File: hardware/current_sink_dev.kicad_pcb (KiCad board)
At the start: 2 copper layers, 80 parts, among them J1 USB_C_Receptacle_USB2.0, Q1 TK7S10N1Z, Q3 TK7S10N1Z, U1 AD8602, U10 STM32F042F6Px, U2 ADTL084, U4 ADTL084, U5 PDSE1-S5-D5-M-TR, U6 ADTL084, U7 MIC5504-1.2YM5, U8 MCP4728, U9 DPO2036

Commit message: Began initial routing. Schematic still not fully complete.
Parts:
- removed C1, C2, C22: ?, Capacitor_SMD:C_0805_2012Metric_Pad1.18x1.45mm_HandSolder
- removed C10, C14, C15, C19: 0.1u, Capacitor_SMD:C_0805_2012Metric_Pad1.18x1.45mm_HandSolder
- removed C11: 10u, Capacitor_SMD:C_0805_2012Metric_Pad1.18x1.45mm_HandSolder
- removed C12, C13, C16, C17, C18, C20, C3: 1u, Capacitor_SMD:C_0805_2012Metric_Pad1.18x1.45mm_HandSolder
- removed C7, C8, C9: 4.7u, Capacitor_SMD:C_0805_2012Metric_Pad1.18x1.45mm_HandSolder
- removed H1, H2, H3, H4: ~, MountingHole:MountingHole_3.2mm_M3_Pad_Via
- removed J1: USB_C_Receptacle_USB2.0, Connector_USB:USB_C_Receptacle_Amphenol_12401610E4-2A
- removed J2: ~, Connector_PinHeader_2.54mm:PinHeader_1x02_P2.54mm_Vertical
- removed Q1, Q3: TK7S10N1Z, Package_TO_SOT_SMD:TO-252-2
- removed R1, R37, R50, R7: 0, Resistor_SMD:R_0805_2012Metric_Pad1.20x1.40mm_HandSolder
- removed R10, R53: 1.9k, Resistor_SMD:R_0805_2012Metric_Pad1.20x1.40mm_HandSolder
- removed R11, R3, R43, R44, R45, R46, R48, R49, R5, R52, R54, R6, R9: 10k, Resistor_SMD:R_0805_2012Metric_Pad1.20x1.40mm_HandSolder
- removed R12, R4, R47, R55: 1k, Resistor_SMD:R_0805_2012Metric_Pad1.20x1.40mm_HandSolder
- removed R13, R14, R15, R2, R38, R56, R57, R58: 100, Resistor_SMD:R_0805_2012Metric_Pad1.20x1.40mm_HandSolder
- removed R31, R32, R33, R34: 0R, Resistor_SMD:R_0805_2012Metric_Pad1.20x1.40mm_HandSolder
- removed R35, R36, R39, R40: R_Small, Resistor_SMD:R_0805_2012Metric_Pad1.20x1.40mm_HandSolder
- removed R41, R42: ?, Resistor_SMD:R_0805_2012Metric_Pad1.20x1.40mm_HandSolder
- removed R51, R8: 100m, Resistor_SMD:R_1206_3216Metric_Pad1.30x1.75mm_HandSolder
- removed RV1, RV3: PT10LV05, Potentiometer_THT:Potentiometer_Piher_PT-10-V05_Vertical
- removed U1: AD8602, Package_SO:MSOP-8_3x3mm_P0.65mm
- removed U10: STM32F042F6Px, Package_SO:TSSOP-20_4.4x6.5mm_P0.65mm
- removed U2, U4, U6: ADTL084, Package_SO:SOIC-14_3.9x8.7mm_P1.27mm
- removed U5: PDSE1-S5-D5-M-TR, User_SupplyGen:PDS1-M
- removed U7: MIC5504-1.2YM5, Package_TO_SOT_SMD:SOT-23-5_HandSoldering
- removed U8: MCP4728, Package_SO:MSOP-10_3x3mm_P0.5mm
- removed U9: DPO2036, User_USB_Protection:UQFN2020-12
- added C100: 4.7u, Capacitor_SMD:C_0805_2012Metric_Pad1.18x1.45mm_HandSolder, B.Cu at (207.5, 32.5)
- added C101: 4.7u, Capacitor_SMD:C_0805_2012Metric_Pad1.18x1.45mm_HandSolder, B.Cu at (214.0, 32.5)
- added C102: 4.7u, Capacitor_SMD:C_0805_2012Metric_Pad1.18x1.45mm_HandSolder, B.Cu at (203.5, 32.5)
- added C200: ?, Capacitor_SMD:C_0805_2012Metric_Pad1.18x1.45mm_HandSolder, F.Cu at (134.0, 97.5)
- added C201: ?, Capacitor_SMD:C_0805_2012Metric_Pad1.18x1.45mm_HandSolder, B.Cu at (133.5, 127.5)
- added C202: ?, Capacitor_SMD:C_0805_2012Metric_Pad1.18x1.45mm_HandSolder, F.Cu at (134.0, 103.5)
- added C203: 1u, Capacitor_SMD:C_0805_2012Metric_Pad1.18x1.45mm_HandSolder, F.Cu at (128.0, 130.0)
- added C204: 1u, Capacitor_SMD:C_0805_2012Metric_Pad1.18x1.45mm_HandSolder, F.Cu at (128.0, 150.0)
- added C300: 1u, Capacitor_SMD:C_0805_2012Metric_Pad1.18x1.45mm_HandSolder, B.Cu at (258.0, 64.0)
- added C400: 0.1u, Capacitor_SMD:C_0805_2012Metric_Pad1.18x1.45mm_HandSolder, F.Cu at (148.8, 75.4)
- added C401: 10u, Capacitor_SMD:C_0805_2012Metric_Pad1.18x1.45mm_HandSolder, F.Cu at (148.8, 78.4)
- added C402: 1u, Capacitor_SMD:C_0805_2012Metric_Pad1.18x1.45mm_HandSolder, F.Cu at (228.0, 76.0)
- added C403: 1u, Capacitor_SMD:C_0805_2012Metric_Pad1.18x1.45mm_HandSolder, F.Cu at (236.0, 76.0)
- added C404: 0.1u, Capacitor_SMD:C_0805_2012Metric_Pad1.18x1.45mm_HandSolder, F.Cu at (148.8, 87.4)
- added C405: 0.1u, Capacitor_SMD:C_0805_2012Metric_Pad1.18x1.45mm_HandSolder, F.Cu at (153.6, 75.4)
- added C406: 1u, Capacitor_SMD:C_0805_2012Metric_Pad1.18x1.45mm_HandSolder, F.Cu at (153.6, 78.4)
- added C407: 1u, Capacitor_SMD:C_0805_2012Metric_Pad1.18x1.45mm_HandSolder, F.Cu at (153.6, 81.4)
- added C408: 1u, Capacitor_SMD:C_0805_2012Metric_Pad1.18x1.45mm_HandSolder, F.Cu at (153.6, 84.4)
- added C409: 0.1u, Capacitor_SMD:C_0805_2012Metric_Pad1.18x1.45mm_HandSolder, F.Cu at (153.6, 87.4)
- added H500: ~, MountingHole:MountingHole_3.2mm_M3_Pad_Via, F.Cu at (225.0, 119.0)
- added H501: ~, MountingHole:MountingHole_3.2mm_M3_Pad_Via, F.Cu at (192.5, 32.5)
- added H502: ~, MountingHole:MountingHole_3.2mm_M3_Pad_Via, F.Cu at (192.5, 117.5)
- added H503: ~, MountingHole:MountingHole_3.2mm_M3_Pad_Via, F.Cu at (257.5, 117.5)
- added H504: ~, MountingHole:MountingHole_3.2mm_M3_Pad_Via, F.Cu at (257.5, 32.5)
- added H505: ~, MountingHole:MountingHole_3.2mm_M3_Pad_Via, F.Cu at (225.0, 109.0)
- added J100: USB_C_Receptacle_USB2.0, Connector_USB:USB_C_Receptacle_Amphenol_12401610E4-2A, F.Cu at (240.5, 29.2)
- added J500: Conn_01x01_Socket, Connector:Banana_Cliff_FCR7350x_S16N-PC_Horizontal, F.Cu at (212.5, 115.0)
- added J501: Conn_01x01_Socket, Connector:Banana_Cliff_FCR7350x_S16N-PC_Horizontal, F.Cu at (237.5, 115.0)
- added J502: ~, Connector_PinHeader_2.54mm:PinHeader_1x02_P2.54mm_Vertical, F.Cu at (57.2, 74.1)
- added Q200: TK7S10N1Z, Package_TO_SOT_SMD:TO-252-2, F.Cu at (167.2, 96.9)
- added Q201: TK7S10N1Z, Package_TO_SOT_SMD:TO-252-2, F.Cu at (167.2, 106.3)
- added R100: 0R, Resistor_SMD:R_0805_2012Metric_Pad1.20x1.40mm_HandSolder, F.Cu at (199.5, 36.0)
- added R200: 0, Resistor_SMD:R_0805_2012Metric_Pad1.20x1.40mm_HandSolder, F.Cu at (102.8, 87.2)
- added R201: 100, Resistor_SMD:R_0805_2012Metric_Pad1.20x1.40mm_HandSolder, F.Cu at (102.8, 90.2)
- added R202: 10k, Resistor_SMD:R_0805_2012Metric_Pad1.20x1.40mm_HandSolder, F.Cu at (128.0, 124.5)
- added R203: 1k, Resistor_SMD:R_0805_2012Metric_Pad1.20x1.40mm_HandSolder, F.Cu at (102.8, 96.1)
- added R204: 10k, Resistor_SMD:R_0805_2012Metric_Pad1.20x1.40mm_HandSolder, F.Cu at (126.0, 124.5)
- added R205: 10k, Resistor_SMD:R_0805_2012Metric_Pad1.20x1.40mm_HandSolder, F.Cu at (126.0, 130.0)
- added R206: 0, Resistor_SMD:R_0805_2012Metric_Pad1.20x1.40mm_HandSolder, F.Cu at (143.0, 130.0)
- added R207: 100m, Resistor_SMD:R_1206_3216Metric_Pad1.30x1.75mm_HandSolder, F.Cu at (110.0, 113.3)
- added R208: 10k, Resistor_SMD:R_0805_2012Metric_Pad1.20x1.40mm_HandSolder, F.Cu at (141.0, 130.0)
- added R209: 1.9k, Resistor_SMD:R_0805_2012Metric_Pad1.20x1.40mm_HandSolder, F.Cu at (115.5, 124.5)
- added R210: 10k, Resistor_SMD:R_0805_2012Metric_Pad1.20x1.40mm_HandSolder, F.Cu at (139.0, 130.0)
- added R211: 1k, Resistor_SMD:R_0805_2012Metric_Pad1.20x1.40mm_HandSolder, F.Cu at (117.5, 124.5)
- added R212: 100, Resistor_SMD:R_0805_2012Metric_Pad1.20x1.40mm_HandSolder, F.Cu at (119.5, 124.5)
- added R213: 100, Resistor_SMD:R_0805_2012Metric_Pad1.20x1.40mm_HandSolder, F.Cu at (115.5, 128.5)
- added R214: 100, Resistor_SMD:R_0805_2012Metric_Pad1.20x1.40mm_HandSolder, F.Cu at (117.5, 128.5)
- added R215: 0, Resistor_SMD:R_0805_2012Metric_Pad1.20x1.40mm_HandSolder, F.Cu at (107.6, 104.9)
- added R216: 100, Resistor_SMD:R_0805_2012Metric_Pad1.20x1.40mm_HandSolder, F.Cu at (107.6, 107.9)
- added R217: 10k, Resistor_SMD:R_0805_2012Metric_Pad1.20x1.40mm_HandSolder, F.Cu at (128.0, 144.5)
- added R218: 1k, Resistor_SMD:R_0805_2012Metric_Pad1.20x1.40mm_HandSolder, F.Cu at (112.3, 90.2)
- added R219: 10k, Resistor_SMD:R_0805_2012Metric_Pad1.20x1.40mm_HandSolder, F.Cu at (126.0, 144.5)
- added R220: 10k, Resistor_SMD:R_0805_2012Metric_Pad1.20x1.40mm_HandSolder, F.Cu at (126.0, 150.0)
- added R221: 0, Resistor_SMD:R_0805_2012Metric_Pad1.20x1.40mm_HandSolder, F.Cu at (143.0, 150.0)
- added R222: 100m, Resistor_SMD:R_1206_3216Metric_Pad1.30x1.75mm_HandSolder, F.Cu at (110.0, 116.0)
- added R223: 10k, Resistor_SMD:R_0805_2012Metric_Pad1.20x1.40mm_HandSolder, F.Cu at (141.0, 150.0)
- added R224: 1.9k, Resistor_SMD:R_0805_2012Metric_Pad1.20x1.40mm_HandSolder, F.Cu at (104.5, 124.5)
- added R225: 10k, Resistor_SMD:R_0805_2012Metric_Pad1.20x1.40mm_HandSolder, F.Cu at (139.0, 150.0)
- added R226: 1k, Resistor_SMD:R_0805_2012Metric_Pad1.20x1.40mm_HandSolder, F.Cu at (102.5, 124.5)
- added R227: 100, Resistor_SMD:R_0805_2012Metric_Pad1.20x1.40mm_HandSolder, F.Cu at (100.5, 124.5)
- added R228: 100, Resistor_SMD:R_0805_2012Metric_Pad1.20x1.40mm_HandSolder, F.Cu at (104.5, 128.5)
- added R229: 100, Resistor_SMD:R_0805_2012Metric_Pad1.20x1.40mm_HandSolder, F.Cu at (102.5, 128.5)
- added R400: ?, Resistor_SMD:R_0805_2012Metric_Pad1.20x1.40mm_HandSolder, F.Cu at (158.4, 75.3)
- added R401: ?, Resistor_SMD:R_0805_2012Metric_Pad1.20x1.40mm_HandSolder, F.Cu at (158.4, 78.3)
- added R402: 10k, Resistor_SMD:R_0805_2012Metric_Pad1.20x1.40mm_HandSolder, F.Cu at (158.4, 81.2)
- added R403: 10k, Resistor_SMD:R_0805_2012Metric_Pad1.20x1.40mm_HandSolder, F.Cu at (158.4, 84.2)
- added R404: 10k, Resistor_SMD:R_0805_2012Metric_Pad1.20x1.40mm_HandSolder, F.Cu at (158.4, 87.1)
- added R500: 0R, Resistor_SMD:R_0805_2012Metric_Pad1.20x1.40mm_HandSolder, F.Cu at (145.0, 124.5)
- added R501: 0R, Resistor_SMD:R_0805_2012Metric_Pad1.20x1.40mm_HandSolder, F.Cu at (143.0, 124.5)
- added R502: R_Small, Resistor_SMD:R_0805_2012Metric_Pad1.20x1.40mm_HandSolder, F.Cu at (139.0, 124.5)
- added R503: R_Small, Resistor_SMD:R_0805_2012Metric_Pad1.20x1.40mm_HandSolder, F.Cu at (141.0, 124.5)
- added R504: 0R, Resistor_SMD:R_0805_2012Metric_Pad1.20x1.40mm_HandSolder, F.Cu at (145.0, 144.5)
- added R505: 0R, Resistor_SMD:R_0805_2012Metric_Pad1.20x1.40mm_HandSolder, F.Cu at (143.0, 144.5)
- added R506: R_Small, Resistor_SMD:R_0805_2012Metric_Pad1.20x1.40mm_HandSolder, F.Cu at (139.0, 144.5)
- added R507: R_Small, Resistor_SMD:R_0805_2012Metric_Pad1.20x1.40mm_HandSolder, F.Cu at (141.0, 144.5)
- added RV200: PT10LV05, Potentiometer_THT:Potentiometer_Piher_PT-10-V05_Vertical, F.Cu at (103.9, 82.3)
- added RV201: PT10LV05, Potentiometer_THT:Potentiometer_Piher_PT-10-V05_Vertical, F.Cu at (115.8, 82.3)
- added RV300: PT10LV05, Potentiometer_THT:Potentiometer_Piher_PT-10-V05_Vertical, B.Cu at (255.5, 51.5)
- added S300: VIM-878-DP-RC-S-LV, User_LDC_Display:VIM878DPRCSLV, F.Cu at (225.0, 55.0)
- added SW500: RotaryEncoder_Switch, Rotary_Encoder:RotaryEncoder_Alps_EC11E-Switch_Vertical_H20mm, F.Cu at (244.8, 88.8)
- added U100: PDSE1-S5-D5-M-TR, User_SupplyGen:PDS1-M, F.Cu at (210.2, 32.5)
- added U200: AD8602, Package_SO:MSOP-8_3x3mm_P0.65mm, F.Cu at (110.0, 126.0)
- added U201: ADTL084, Package_SO:SOIC-14_3.9x8.7mm_P1.27mm, F.Cu at (133.5, 127.3)
- added U202: ADTL084, Package_SO:SOIC-14_3.9x8.7mm_P1.27mm, F.Cu at (133.5, 147.5)
- added U300: BU9797A, Package_SO:TSSOP-48_8x12.5mm_P0.5mm, B.Cu at (225.0, 55.0)
- added U400: MIC5504-1.2YM5, Package_TO_SOT_SMD:SOT-23-5_HandSoldering, F.Cu at (232.0, 76.0)
- added U401: MCP4728, Package_SO:MSOP-10_3x3mm_P0.5mm, F.Cu at (237.1, 84.7)
- added U402: DPO2036, User_USB_Protection:UQFN2020-12, F.Cu at (225.5, 32.2)
- added U403: STM32F042F6Px, Package_SO:TSSOP-20_4.4x6.5mm_P0.65mm, F.Cu at (282.5, 87.0)
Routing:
- net /LCD_screen/disp36_dig_l: track 0.00 -> 48.4 mm, vias 0 -> 2
- net /LCD_screen/disp35_dig_l: track 0.00 -> 45.7 mm, vias 0 -> 2
- net /LCD_screen/disp1_dig_l: track 0.00 -> 45.7 mm, vias 0 -> 2
- net /LCD_screen/disp2_dig_l: track 0.00 -> 43.0 mm, vias 0 -> 2
- net /LCD_screen/disp34_dig_l: track 0.00 -> 40.6 mm, vias 0 -> 2
- net /LCD_screen/disp3_dig_l: track 0.00 -> 38.8 mm, vias 0 -> 2
- net /LCD_screen/disp4_dig_l: track 0.00 -> 37.5 mm, vias 0 -> 2
- net /LCD_screen/disp5_dig_l: track 0.00 -> 36.4 mm, vias 0 -> 2
- net /LCD_screen/disp33_dig_l: track 0.00 -> 35.6 mm, vias 0 -> 2
- net /LCD_screen/COM1_dig_l: track 0.00 -> 33.2 mm, vias 0 -> 2
- net /LCD_screen/COM0_dig_l: track 0.00 -> 32.8 mm, vias 0 -> 2
- net /LCD_screen/disp6_dig_l: track 0.00 -> 30.4 mm, vias 0 -> 2
- net /LCD_screen/disp32_dig_l: track 0.00 -> 30.2 mm, vias 0 -> 2
- net /LCD_screen/disp21_dig_l: track 0.00 -> 28.3 mm
- net /LCD_screen/disp16_dig_l: track 0.00 -> 27.6 mm
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- added copper zone on B.Cu, net GND
- added copper zone on F.Cu, net GND
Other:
- board outline added: 80 x 100 mm

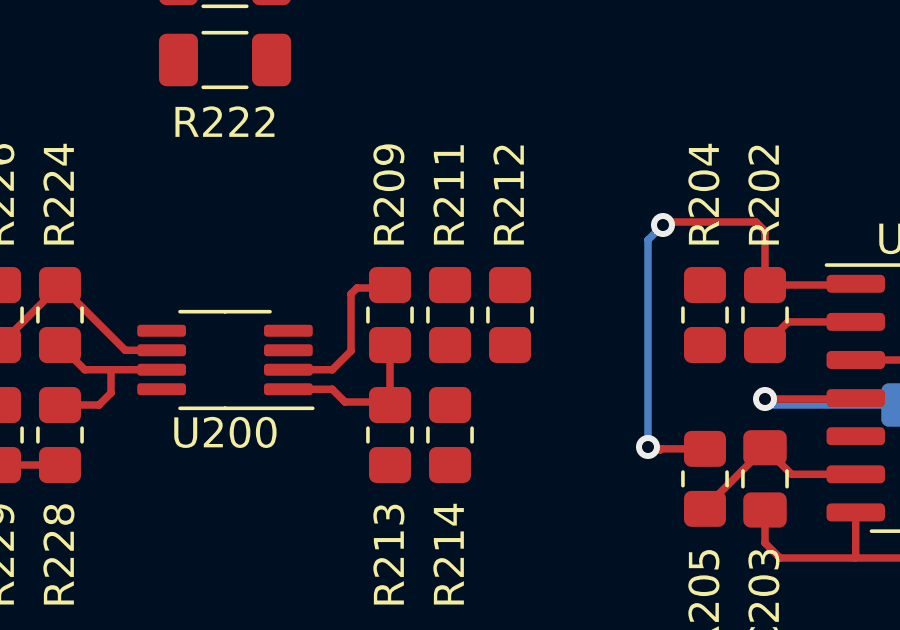
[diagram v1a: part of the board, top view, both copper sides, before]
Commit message: Changed to 4 layer design.
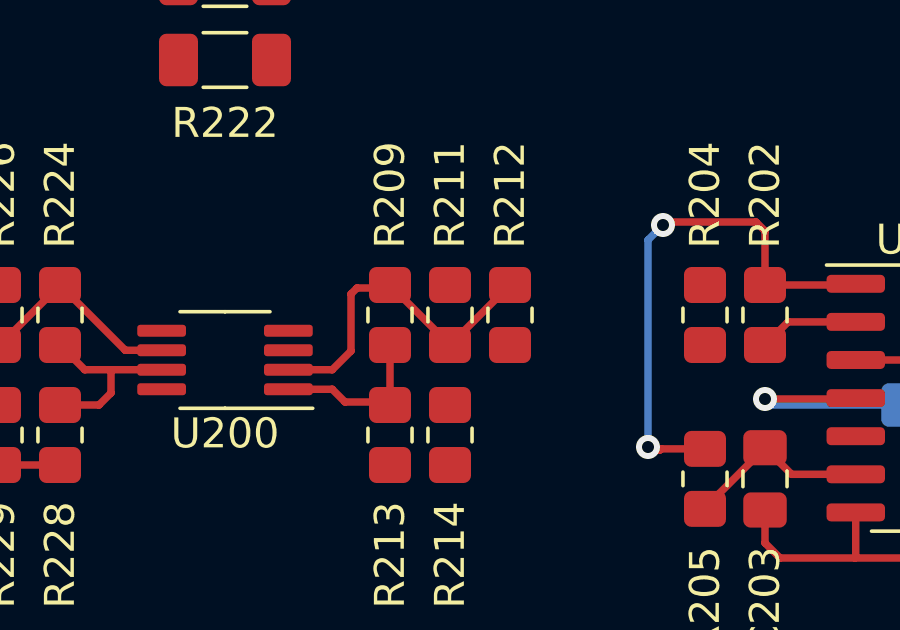
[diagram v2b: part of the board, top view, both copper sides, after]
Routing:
- net Net-(U200A--): track 5.67 -> 11.3 mm
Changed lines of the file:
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@@
   (segment (start 139 129) (end 141 129) (width 0.25) (layer "F.Cu") (net 81))
   (segment (start 114.4 123.6) (end 115.4 123.6) (width 0.25) (layer "F.Cu") (net 82))
+  (segment (start 117.5 125.5) (end 119.5 123.5) (width 0.25) (layer "F.Cu") (net 82))
   (segment (start 112.1125 126.325) (end 113.575 126.325) (width 0.25) (layer "F.Cu") (net 82))
   (segment (start 114.2 125.7) (end 114.2 123.8) (width 0.25) (layer "F.Cu") (net 82))
+  (segment (start 115.5 123.5) (end 117.5 125.5) (width 0.25) (layer "F.Cu") (net 82))
   (segment (start 114.2 123.8) (end 114.4 123.6) (width 0.25) (layer "F.Cu") (net 82))
   (segment (start 113.575 126.325) (end 114.2 125.7) (width 0.25) (layer "F.Cu") (net 82))

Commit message: Routing close to completion. Pending review.
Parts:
- removed R211, R226: 1k, Resistor_SMD:R_0805_2012Metric_Pad1.20x1.40mm_HandSolder
- removed R400, R401: ?, Resistor_SMD:R_0805_2012Metric_Pad1.20x1.40mm_HandSolder
- removed RV200, RV201: PT10LV05, Potentiometer_THT:Potentiometer_Piher_PT-10-V05_Vertical
- added H506: ~, MountingHole:MountingHole_2.2mm_M2_ISO7380_Pad_TopOnly, B.Cu at (96.5, 100.1)
- added H507: ~, MountingHole:MountingHole_2.2mm_M2_ISO7380_Pad_TopOnly, B.Cu at (108.5, 100.1)
- added H508: ~, MountingHole:MountingHole_2.2mm_M2_ISO7380_Pad_TopOnly, B.Cu at (96.5, 123.1)
- added H509: ~, MountingHole:MountingHole_2.2mm_M2_ISO7380_Pad_TopOnly, B.Cu at (108.5, 123.1)
- added J503: 5V_IN, Connector_PinSocket_2.54mm:PinSocket_1x02_P2.54mm_Vertical, F.Cu at (157.0, 44.4)
- added R508: 0R, Resistor_SMD:R_0805_2012Metric_Pad1.20x1.40mm_HandSolder, F.Cu at (134.4, 41.6)
- added R509: 0R, Resistor_SMD:R_0805_2012Metric_Pad1.20x1.40mm_HandSolder, F.Cu at (136.4, 41.6)
- added R510: ?, Resistor_SMD:R_0805_2012Metric_Pad1.20x1.40mm_HandSolder, F.Cu at (100.3, 86.5)
- added R511: ?, Resistor_SMD:R_0805_2012Metric_Pad1.20x1.40mm_HandSolder, F.Cu at (100.3, 88.5)
- added TP500: ~, TestPoint:TestPoint_Pad_D1.0mm, F.Cu at (102.4, 59.6)
- added TP501: ~, TestPoint:TestPoint_Pad_D1.0mm, F.Cu at (106.0, 40.5)
- added TP502: ~, TestPoint:TestPoint_Pad_D1.0mm, F.Cu at (127.7, 46.5)
- added TP503: ~, TestPoint:TestPoint_Pad_D1.0mm, F.Cu at (144.5, 86.0)
- added TP504: ~, TestPoint:TestPoint_Pad_D1.0mm, F.Cu at (120.5, 86.0)
- added TP505: ~, TestPoint:TestPoint_Pad_D1.0mm, F.Cu at (136.2, 103.8)
- added TP506: ~, TestPoint:TestPoint_Pad_D1.0mm, F.Cu at (120.5, 88.0)
- added TP507: ~, TestPoint:TestPoint_Pad_D1.0mm, F.Cu at (161.9, 59.2)
- added TP508: ~, TestPoint:TestPoint_Pad_D1.0mm, F.Cu at (97.1, 94.8)
- added TP509: ~, TestPoint:TestPoint_Pad_D1.0mm, F.Cu at (126.5, 43.0)
- added TP510: ~, TestPoint:TestPoint_Pad_D1.0mm, F.Cu at (147.9, 114.0)
- added TP511: ~, TestPoint:TestPoint_Pad_D1.0mm, F.Cu at (150.1, 114.0)
- added TP512: ~, TestPoint:TestPoint_Pad_D1.0mm, F.Cu at (163.0, 114.0)
- added TP513: ~, TestPoint:TestPoint_Pad_D1.0mm, F.Cu at (170.2, 94.1)
- added TP514: ~, TestPoint:TestPoint_Pad_D1.0mm, F.Cu at (126.4, 117.7)
- added TP515: ~, TestPoint:TestPoint_Pad_D1.0mm, F.Cu at (150.1, 92.7)
- added TP516: ~, TestPoint:TestPoint_Pad_D1.0mm, F.Cu at (150.1, 94.8)
- added TP517: ~, TestPoint:TestPoint_Pad_D1.0mm, F.Cu at (122.7, 110.0)
- added TP518: ~, TestPoint:TestPoint_Pad_D1.0mm, F.Cu at (120.0, 96.4)
- added TP519: 3V3, TestPoint:TestPoint_Pad_D1.0mm, F.Cu at (96.5, 73.5)
- added TP520: SWDIO, TestPoint:TestPoint_Pad_D1.0mm, F.Cu at (96.5, 78.7)
- added TP521: SWDCLK, TestPoint:TestPoint_Pad_D1.0mm, F.Cu at (96.5, 76.2)
- added TP522: GND, TestPoint:TestPoint_Pad_D1.0mm, F.Cu at (96.5, 81.3)
- C200, C202, R100, R209, R212, R213, R214, R224, R227, R228, R229, U200: moved to B.Cu
- C300, RV300: moved to F.Cu
- moved U403 172.0 mm to (110.5, 91.0)
- moved C403 139.2 mm to (97.9, 58.5), turned to 0 degrees
- moved U400 134.8 mm to (98.0, 61.5), turned to 180 degrees
- moved C402 130.5 mm to (98.0, 64.5), turned to 0 degrees
- moved SW500 97.2 mm to (148.5, 102.0)
- moved U402 94.0 mm to (132.5, 46.0)
- moved S300 93.9 mm to (132.0, 68.1)
- moved C100 93.9 mm to (114.5, 45.5)
- moved C101 93.9 mm to (121.0, 45.5)
- moved C102 93.9 mm to (110.5, 45.5)
- moved H500 93.9 mm to (132.0, 131.9)
- moved H501 93.9 mm to (99.5, 45.5)
- moved H502 93.9 mm to (99.5, 130.5)
- moved H503 93.9 mm to (164.5, 130.5)
- moved H504 93.9 mm to (164.5, 45.5)
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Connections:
- net Net-(U100-VIN) renamed /supply_gen/usb5v_l
- C101 pad 2: GND1 -> GND
- C406 pad 1: /uC_stage/3V3_SUPPLY_L -> 3V3_SUPPLY_G
- SW500 pad A: unconnected-(SW500-PadA) -> /uC_stage/encoderA_dig_l
- SW500 pad B: unconnected-(SW500-PadB) -> /uC_stage/encoderB_dig_l
- SW500 pad C: unconnected-(SW500-PadC) -> GND
- SW500 pad S1: unconnected-(SW500-PadS1) -> /uC_stage/encoderSW_dig_l
- SW500 pad S2: unconnected-(SW500-PadS2) -> GND
- U100 pad 1: GND1 -> GND
- U402 pad 12: /uC_stage/3V3_SUPPLY_L -> 3V3_SUPPLY_G
- U403 pad 1: unconnected-(U403-PB8-Pad1) -> UCSCL_COM_G
- U403 pad 10: unconnected-(U403-PA4-Pad10) -> /uC_stage/dacNLDAC_dig_l
- U403 pad 11: unconnected-(U403-PA5-Pad11) -> opStage2A_ang_g
- U403 pad 12: unconnected-(U403-PA6-Pad12) -> opStage2B_ang_g
- U403 pad 17: unconnected-(U403-PA9/PA11-Pad17) -> USB_C_ISOLATED_DNEG
- U403 pad 18: unconnected-(U403-PA10/PA12-Pad18) -> USB_C_ISOLATED_DPOS
- U403 pad 19: unconnected-(U403-PA13-Pad19) -> /uC_stage/swdio_com_l
- U403 pad 2: unconnected-(U403-PF0-Pad2) -> UCSDA_COM_G
- U403 pad 20: unconnected-(U403-PA14-Pad20) -> /uC_stage/swdclk_com_l
- U403 pad 6: unconnected-(U403-PA0-Pad6) -> /uC_stage/encoderA_dig_l
- U403 pad 7: unconnected-(U403-PA1-Pad7) -> /uC_stage/encoderB_dig_l
- U403 pad 8: unconnected-(U403-PA2-Pad8) -> /uC_stage/encoderSW_dig_l
- U403 pad 9: unconnected-(U403-PA3-Pad9) -> /uC_stage/dacRDY_dig_l
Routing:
- net UCSDA_COM_G: track 0.00 -> 126.5 mm, vias 0 -> 4
- net UCSCL_COM_G: track 0.00 -> 124.7 mm, vias 0 -> 4
- net GND: track 0.00 -> 101.5 mm, vias 0 -> 34
- net /uC_stage/dacRDY_dig_l: track 0.00 -> 98.8 mm, vias 0 -> 2
- net /uC_stage/dacNLDAC_dig_l: track 0.00 -> 94.0 mm, vias 0 -> 2
- net /uC_stage/encoderSW_dig_l: track 0.00 -> 90.9 mm, vias 0 -> 4
- net /uC_stage/encoderB_dig_l: track 0.00 -> 88.4 mm, vias 0 -> 4
- net /uC_stage/encoderA_dig_l: track 0.00 -> 84.5 mm, vias 0 -> 4
- net dacOutB_ang_g: track 0.00 -> 78.8 mm, vias 0 -> 2
- net USB_C_ISOLATED_DPOS: track 0.00 -> 78.6 mm, vias 0 -> 3
- net USB_C_ISOLATED_DNEG: track 0.00 -> 76.5 mm, vias 0 -> 3
- net dacOutA_ang_g: track 0.00 -> 52.7 mm, vias 0 -> 2
- net Net-(R219-Pad2): track 6.37 -> 54.8 mm, vias 0 -> 3
- net Net-(U300-VDD): track 0.00 -> 44.2 mm, vias 0 -> 1
- net opStage2A_ang_g: track 0.00 -> 40.4 mm, vias 0 -> 2
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- added copper zone on F.Cu, net -5V0_SUPPLY_G
- added copper zone on In2.Cu, net -5V0_SUPPLY_G
- added copper zone on F.Cu, net /current_sink_stage/current_feedback_A
- added copper zone on F.Cu, net /current_sink_stage/current_feedback_B
- added copper zone on In2.Cu, net /supply_gen/usb5v_l
- added copper zone on F.Cu, net 3V3_SUPPLY_G
- added copper zone on In2.Cu, net 3V3_SUPPLY_G
- added copper zone on F.Cu, net 5V0_SUPPLY_G
- added copper zone on In2.Cu, net 5V0_SUPPLY_G
- added copper zone on In1.Cu, net GND
- added copper zone on F.Cu, net VOLTAGE_SINK_G
- added copper zone on In2.Cu, net VOLTAGE_SINK_G
- removed copper zone on B.Cu, net GND
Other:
- outline, holes or cut-outs redrawn
- copper layers 2 -> 4
- board text added: "5V IN"
- board text added: "BYPASS U402"
- board text added: "GND"
- board text added: "SINK"

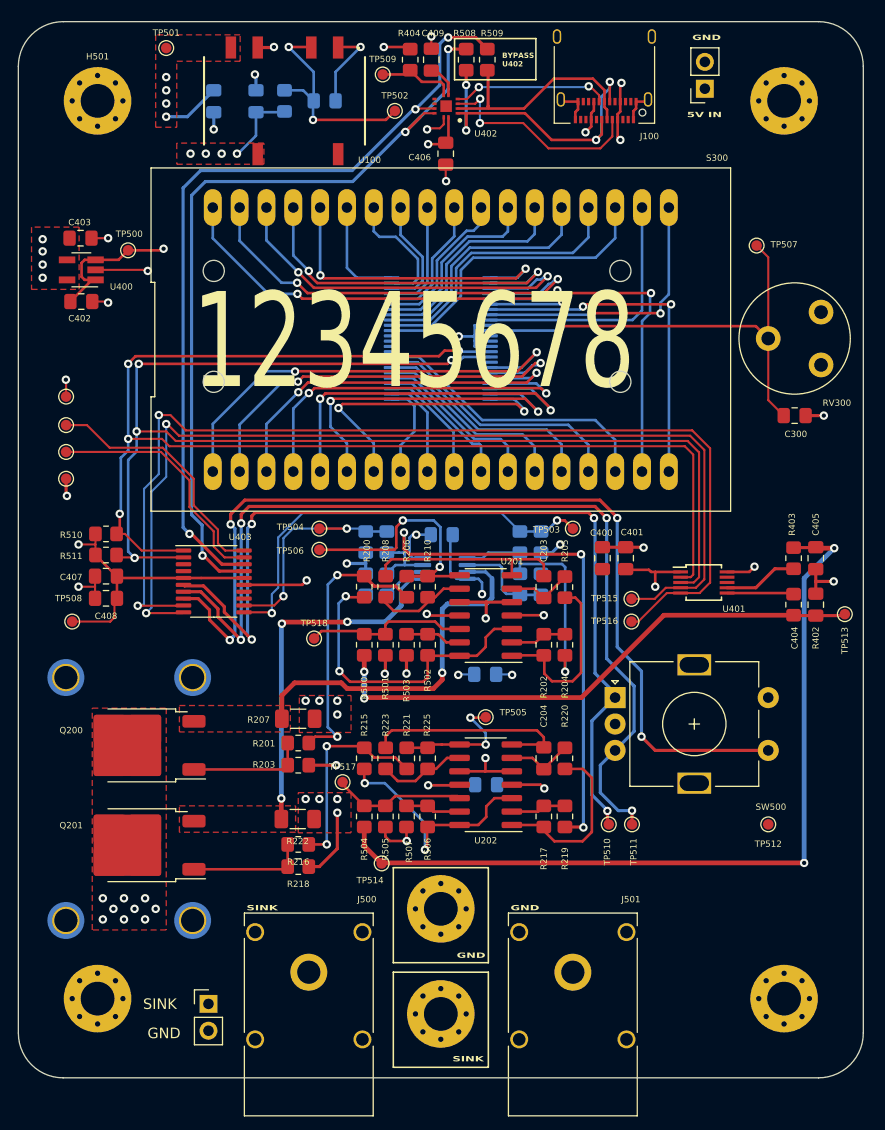
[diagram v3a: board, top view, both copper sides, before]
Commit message: Started programming LCD interface
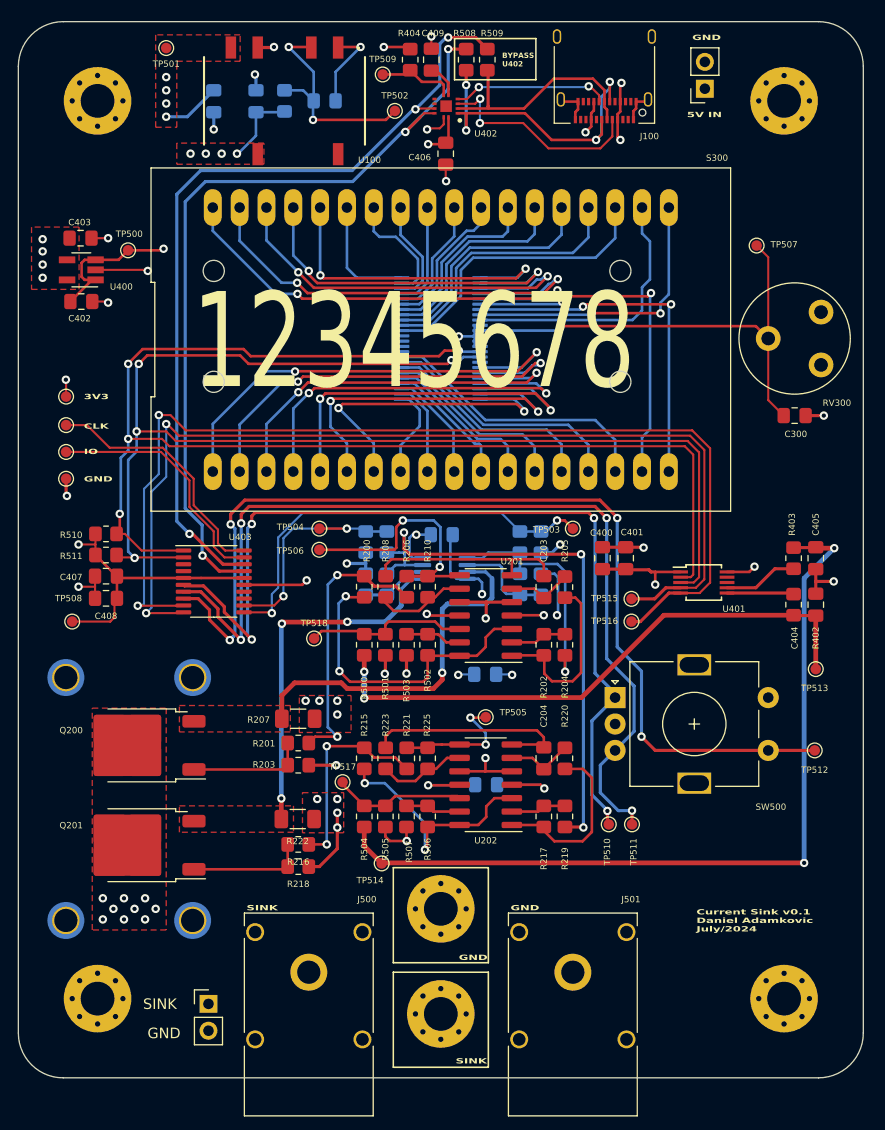
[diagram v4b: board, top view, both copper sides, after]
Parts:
- added G***: LOGO, LOGO, B.Cu at (160.2, 119.2)
- U300: footprint Package_SO:TSSOP-48_8x12.5mm_P0.5mm -> Package_SO:TSSOP-48_6.1x12.5mm_P0.5mm
- moved TP512 8.27 mm to (167.4, 107.0)
- moved TP513 5.88 mm to (167.5, 99.3)
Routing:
- net /uC_stage/encoderSW_dig_l: track 90.9 -> 95.3 mm
- net dacOutA_ang_g: track 52.7 -> 55.1 mm
- net Net-(U200B--): track 4.29 -> 6.29 mm
- net 3V3_SUPPLY_G: track 40.3 -> 42.3 mm
- net /LCD_screen/disp9_dig_l: track 9.62 -> 8.05 mm
- net /LCD_screen/COM3_dig_l: track 24.6 -> 26.2 mm
- net /LCD_screen/disp8_dig_l: track 9.07 -> 8.05 mm
- net /LCD_screen/disp5_dig_l: track 36.3 -> 37.3 mm
- net Net-(U300-VDD): track 44.2 -> 45.1 mm
- net /LCD_screen/disp7_dig_l: track 29.2 -> 30.1 mm
- net /LCD_screen/disp6_dig_l: track 32.7 -> 33.7 mm
- net /LCD_screen/disp4_dig_l: track 36.6 -> 37.5 mm
- net /LCD_screen/disp3_dig_l: track 36.6 -> 37.5 mm
- net /LCD_screen/disp35_dig_l: track 43.0 -> 43.9 mm
- net /LCD_screen/disp34_dig_l: track 38.1 -> 39.0 mm
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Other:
- board text added: "3V3"
- board text added: "CLK"
- board text added: "Current Sink v0.1 Daniel Adamkovic July/2024"
- board text added: "IO"
